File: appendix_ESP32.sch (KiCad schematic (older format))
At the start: 11 parts, among them Q301 2N3904, Q302 2N3904, SW301 SW_Push, SW302 SW_Push, U301 ESP32-WROOM-32

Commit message: fixed missing symbol issue fixed 3vout cap on FTDI
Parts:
- removed Q301, Q302: 2N3904, digikey-footprints:TO-92-3, symbol dk_Transistors-Bipolar-BJT-Single:2N3904
- added Q1, Q2: 2N3904, Package_TO_SOT_THT:TO-92_Inline, symbol Transistor_BJT:2N3904
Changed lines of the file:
@@
 	5050 4850 5050 4700
-$Comp
-L dk_Transistors-Bipolar-BJT-Single:2N3904 Q301
-U 1 1 5CBEF82D
-P 9500 2350
-F 0 "Q301" H 9688 2403 60  0000 L CNN
-F 1 "2N3904" H 9688 2297 60  0000 L CNN
-F 2 "digikey-footprints:TO-92-3" H 9700 2550 60  0001 L CNN
-F 3 "https://my.centralsemi.com/get_document.php?cmp=1&mergetype=pd&mergepath=pd&pdf_id=LSSGP072.PDF" H 9700 2650 60  0001 L CNN
-F 4 "2N3904CS-ND" H 9700 2750 60  0001 L CNN "Digi-Key_PN"
-F 5 "2N3904" H 9700 2850 60  0001 L CNN "MPN"
-F 6 "Discrete Semiconductor Products" H 9700 2950 60  0001 L CNN "Category"
-F 7 "Transistors - Bipolar (BJT) - Single" H 9700 3050 60  0001 L CNN "Family"
-F 8 "https://my.centralsemi.com/get_document.php?cmp=1&mergetype=pd&mergepath=pd&pdf_id=LSSGP072.PDF" H 9700 3150 60  0001 L CNN "DK_Datasheet_Link"
-F 9 "/product-detail/en/central-semiconductor-corp/2N3904/2N3904CS-ND/4806876" H 9700 3250 60  0001 L CNN "DK_Detail_Page"
-F 10 "TRANS NPN 40V TO-92" H 9700 3350 60  0001 L CNN "Description"
-F 11 "Central Semiconductor Corp" H 9700 3450 60  0001 L CNN "Manufacturer"
-F 12 "Active" H 9700 3550 60  0001 L CNN "Status"
-	1    9500 2350
-	1    0    0    -1
-$EndComp
-$Comp
-L dk_Transistors-Bipolar-BJT-Single:2N3904 Q302
-U 1 1 5CBF1B4A
-P 9500 3000
-F 0 "Q302" H 9688 2947 60  0000 L CNN
-F 1 "2N3904" H 9688 3053 60  0000 L CNN
-F 2 "digikey-footprints:TO-92-3" H 9700 3200 60  0001 L CNN
-F 3 "https://my.centralsemi.com/get_document.php?cmp=1&mergetype=pd&mergepath=pd&pdf_id=LSSGP072.PDF" H 9700 3300 60  0001 L CNN
-F 4 "2N3904CS-ND" H 9700 3400 60  0001 L CNN "Digi-Key_PN"
-F 5 "2N3904" H 9700 3500 60  0001 L CNN "MPN"
-F 6 "Discrete Semiconductor Products" H 9700 3600 60  0001 L CNN "Category"
-F 7 "Transistors - Bipolar (BJT) - Single" H 9700 3700 60  0001 L CNN "Family"
-F 8 "https://my.centralsemi.com/get_document.php?cmp=1&mergetype=pd&mergepath=pd&pdf_id=LSSGP072.PDF" H 9700 3800 60  0001 L CNN "DK_Datasheet_Link"
-F 9 "/product-detail/en/central-semiconductor-corp/2N3904/2N3904CS-ND/4806876" H 9700 3900 60  0001 L CNN "DK_Detail_Page"
-F 10 "TRANS NPN 40V TO-92" H 9700 4000 60  0001 L CNN "Description"
-F 11 "Central Semiconductor Corp" H 9700 4100 60  0001 L CNN "Manufacturer"
-F 12 "Active" H 9700 4200 60  0001 L CNN "Status"
-	1    9500 3000
-	1    0    0    1
-$EndComp
 $Comp
 L Device:R R302
@@
 EndData
 $EndBitmap
+$Comp
+L Transistor_BJT:2N3904 Q1
+U 1 1 5CBE1CFC
+P 9500 2350
+F 0 "Q1" H 9690 2396 50  0000 L CNN
+F 1 "2N3904" H 9690 2305 50  0000 L CNN
+F 2 "Package_TO_SOT_THT:TO-92_Inline" H 9700 2275 50  0001 L CIN
+F 3 "https://www.fairchildsemi.com/datasheets/2N/2N3904.pdf" H 9500 2350 50  0001 L CNN
+	1    9500 2350
+	1    0    0    -1
+$EndComp
+$Comp
+L Transistor_BJT:2N3904 Q2
+U 1 1 5CBE30DA
+P 9500 3000
+F 0 "Q2" H 9690 2954 50  0000 L CNN
+F 1 "2N3904" H 9690 3045 50  0000 L CNN
+F 2 "Package_TO_SOT_THT:TO-92_Inline" H 9700 2925 50  0001 L CIN
+F 3 "https://www.fairchildsemi.com/datasheets/2N/2N3904.pdf" H 9500 3000 50  0001 L CNN
+	1    9500 3000
+	1    0    0    1
+$EndComp
 $EndSCHEMATC

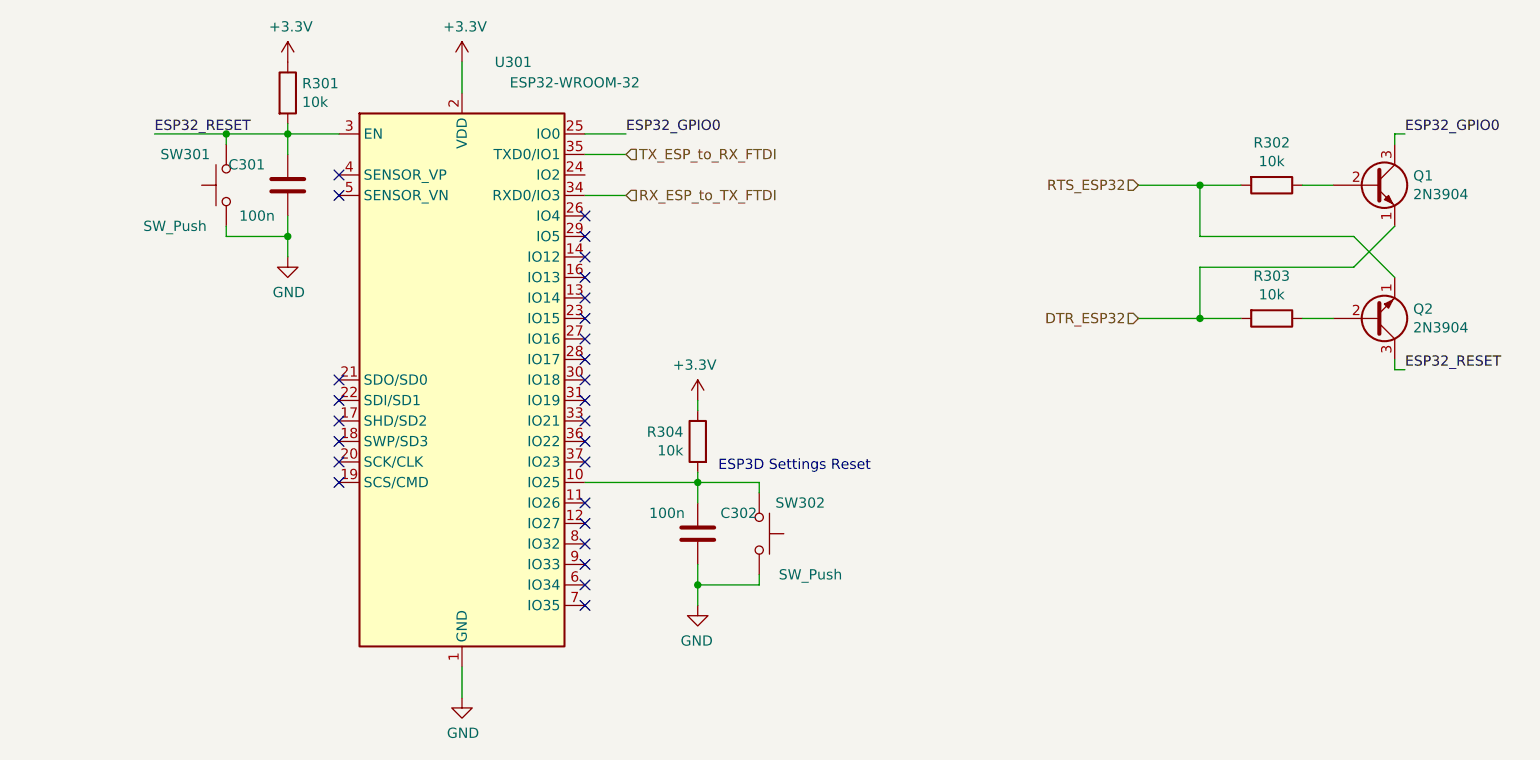
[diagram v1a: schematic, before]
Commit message: started with STM32 Pinout connections (Mittagspause)
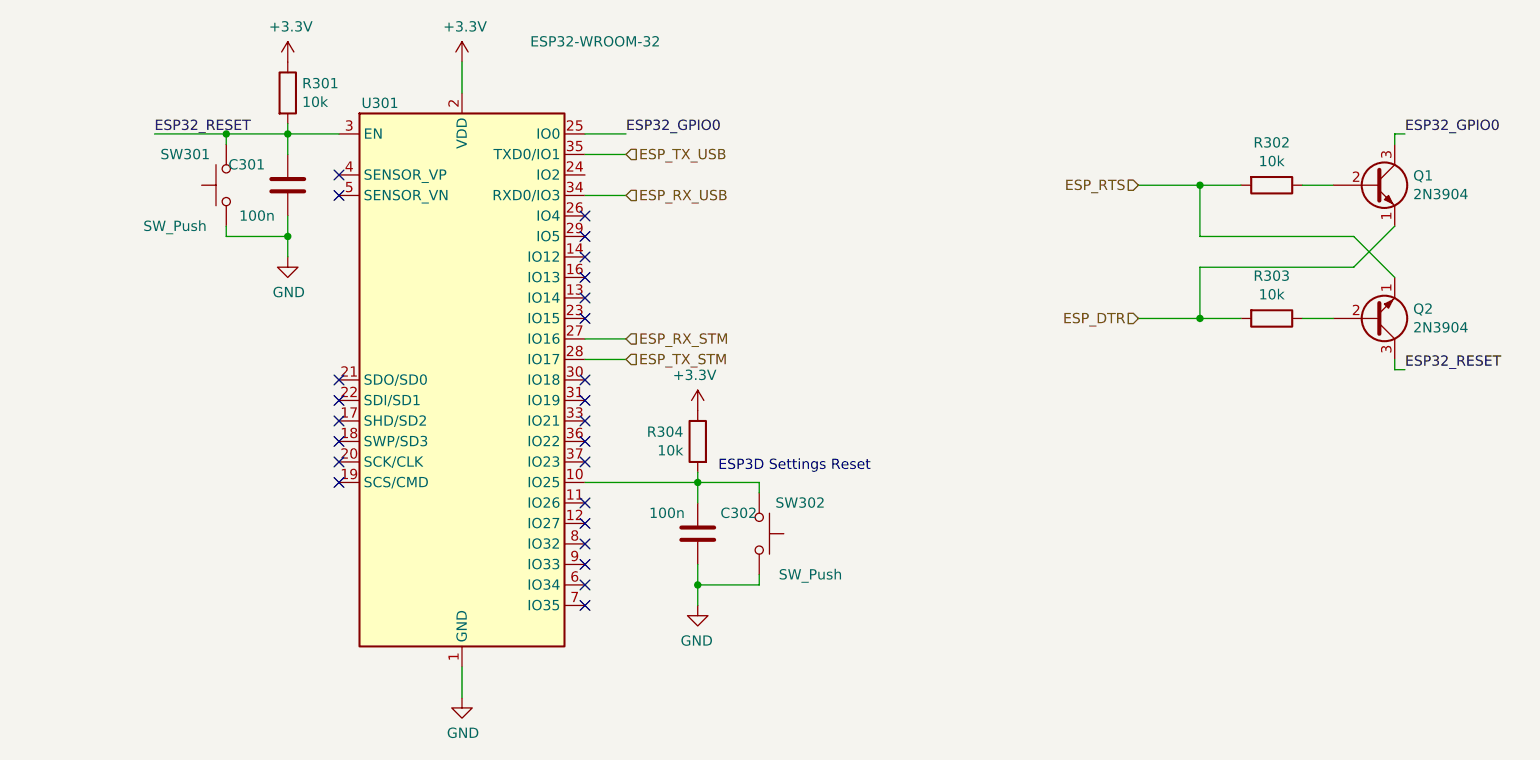
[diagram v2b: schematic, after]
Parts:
- Q1, Q2: footprint Package_TO_SOT_THT:TO-92_Inline -> TO_SOT_Packages_SMD:SOT-23
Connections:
- net ESP_RX_STM: now reaches U301.27 (IO16)
- net ESP_TX_STM: now reaches U301.28 (IO17)
- net DTR_ESP32 renamed ESP_DTR
- net RTS_ESP32 renamed ESP_RTS
- net RX_ESP_to_TX_FTDI renamed ESP_RX_USB
- net TX_ESP_to_RX_FTDI renamed ESP_TX_USB
- no-connect marks 27 -> 25

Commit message: having issues with netclasses
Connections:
- no-connect marks 25 -> 26
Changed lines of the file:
@@
 Text HLabel 5850 3200 2    50   Input ~ 0
 ESP_TX_STM
+NoConn ~ 5650 2300
 $EndSCHEMATC

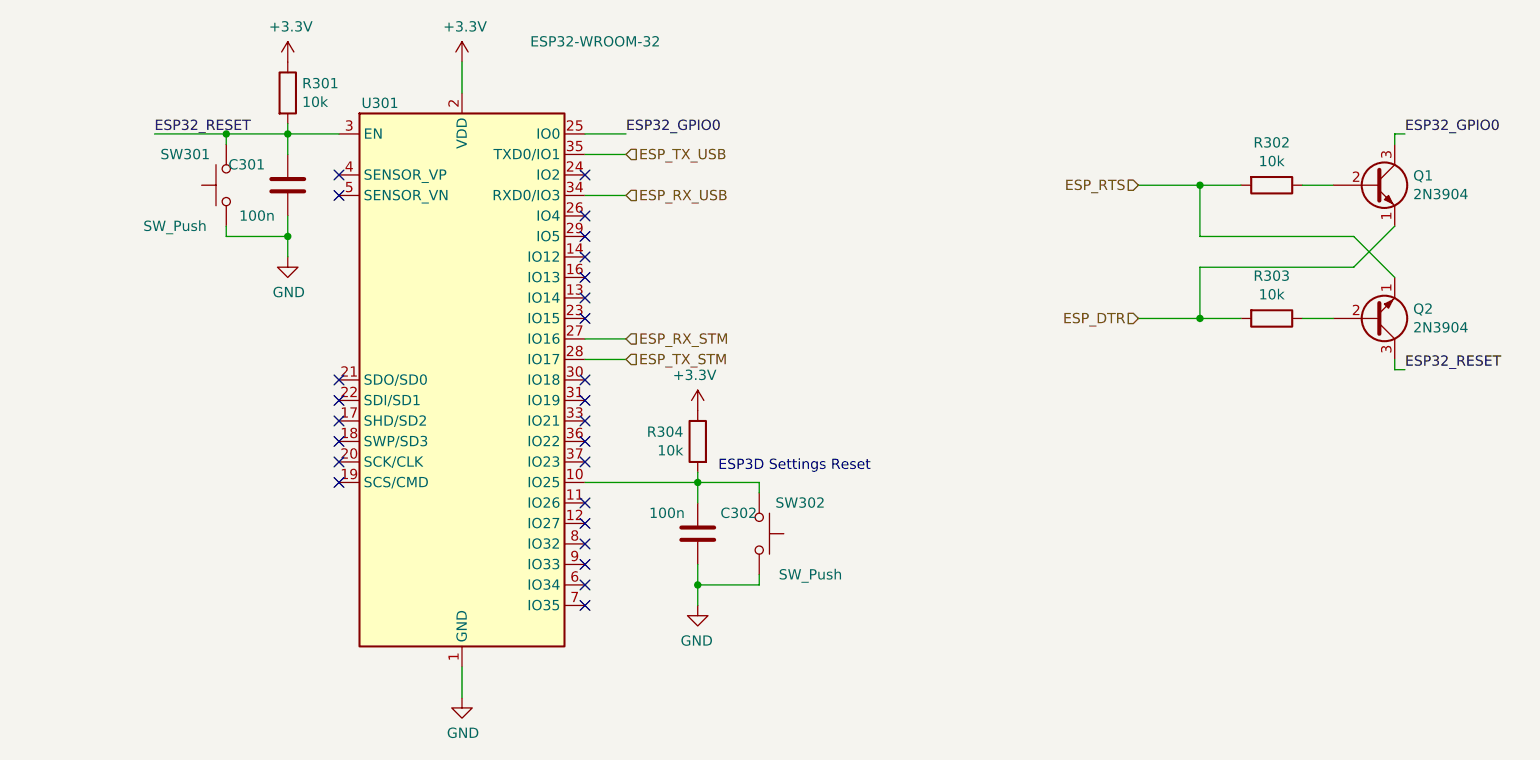
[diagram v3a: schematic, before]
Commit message: TVS protection, BOOT1 pin, user BTN
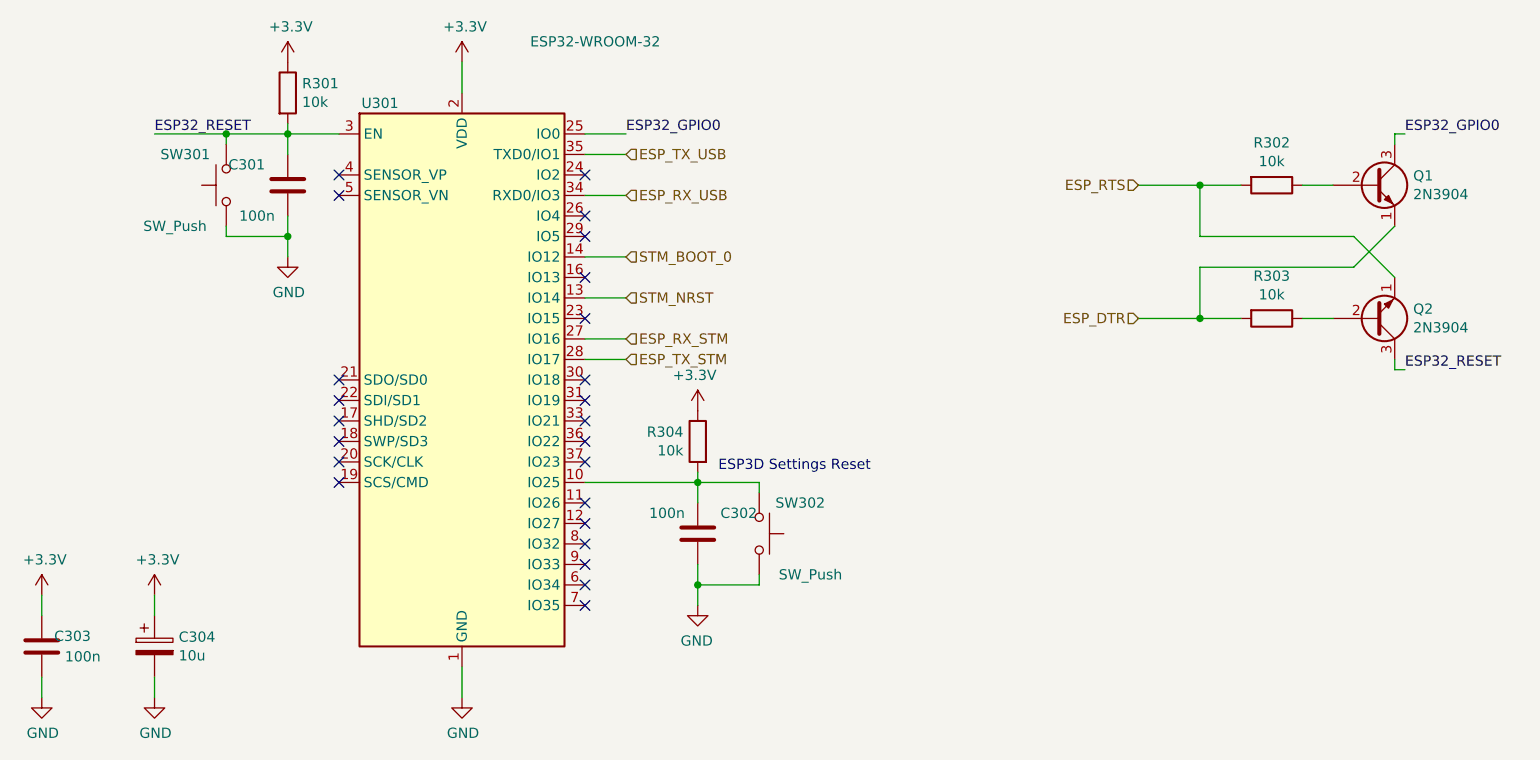
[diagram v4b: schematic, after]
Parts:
- added C303: 100n, Capacitors_SMD:C_0603, symbol Device:C
- added C304: 10u, Capacitors_SMD:C_1210, symbol Device:CP
- SW301, SW302: footprint Button_Switch_SMD:SW_SPST_KMR2 -> Buttons_Switches_SMD:SW_SPST_KMR2
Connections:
- net +3V3: now also C303.1, C304.1
- net GND: now also C303.2, C304.2
- net STM_NRST: now reaches U301.13 (IO14)
- net STM_BOOT_0: now reaches U301.14 (IO12)
- no-connect marks 26 -> 24
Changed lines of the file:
@@
 F 0 "SW302" V 6650 4250 50  0000 C CNN
 F 1 "SW_Push" V 6300 4300 50  0000 C CNN
-F 2 "Button_Switch_SMD:SW_SPST_KMR2" H 6500 4250 50  0001 C CNN
+F 2 "Buttons_Switches_SMD:SW_SPST_KMR2" H 6500 4250 50  0001 C CNN
 F 3 "~" H 6500 4250 50  0001 C CNN
 	1    6500 4050
@@
 F 0 "SW301" V 4050 2550 50  0000 C CNN
 F 1 "SW_Push" V 3700 2600 50  0000 C CNN
-F 2 "Button_Switch_SMD:SW_SPST_KMR2" H 3900 2550 50  0001 C CNN
+F 2 "Buttons_Switches_SMD:SW_SPST_KMR2" H 3900 2550 50  0001 C CNN
 F 3 "~" H 3900 2550 50  0001 C CNN
 	1    3900 2350
@@
 NoConn ~ 5650 3300
 NoConn ~ 5650 3000
-NoConn ~ 5650 2900
 NoConn ~ 5650 2800
-NoConn ~ 5650 2700
 NoConn ~ 5650 2600
 NoConn ~ 5650 2500
@@
 ESP_TX_STM
 NoConn ~ 5650 2300
+$Comp
+L power:GND #PWR?
+U 1 1 5D7E31F6
+P 3550 4850
+AR Path="/5CA3CC17/5D7E31F6" Ref="#PWR?"  Part="1"
+AR Path="/5CA3954A/5D7E31F6" Ref="#PWR?"  Part="1"
+AR Path="/5CA395A8/5D7E31F6" Ref="#PWR0307"  Part="1"
+F 0 "#PWR0307" H 3550 4600 50  0001 C CNN
+F 1 "GND" H 3555 4677 50  0000 C CNN
+F 2 "" H 3550 4850 50  0001 C CNN
+F 3 "" H 3550 4850 50  0001 C CNN
+	1    3550 4850
+	1    0    0    -1
+$EndComp
+Wire Wire Line
+	3550 4450 3550 4350
+Wire Wire Line
+	3550 4850 3550 4750
+$Comp
+L Device:CP C?
+U 1 1 5D7E31FE
+P 3550 4600
+AR Path="/5CA3CC17/5D7E31FE" Ref="C?"  Part="1"
+AR Path="/5CA3954A/5D7E31FE" Ref="C?"  Part="1"
+AR Path="/5CA395A8/5D7E31FE" Ref="C304"  Part="1"
+F 0 "C304" H 3668 4646 50  0000 L CNN
+F 1 "10u" H 3668 4555 50  0000 L CNN
+F 2 "Capacitors_SMD:C_1210" H 3588 4450 50  0001 C CNN
+F 3 "~" H 3550 4600 50  0001 C CNN
+	1    3550 4600
+	1    0    0    -1
+$EndComp
+$Comp
+L power:+3.3V #PWR?
+U 1 1 5D7E3204
+P 3550 4350
+AR Path="/5CA3954A/5D7E3204" Ref="#PWR?"  Part="1"
+AR Path="/5CA395A8/5D7E3204" Ref="#PWR0305"  Part="1"
+F 0 "#PWR0305" H 3550 4200 50  0001 C CNN
+F 1 "+3.3V" H 3565 4523 50  0000 C CNN
+F 2 "" H 3550 4350 50  0001 C CNN
+F 3 "" H 3550 4350 50  0001 C CNN
+	1    3550 4350
+	1    0    0    -1
+$EndComp
+$Comp
+L power:GND #PWR?
+U 1 1 5D7E3B0F
+P 3000 4850
+AR Path="/5CA3CC17/5D7E3B0F" Ref="#PWR?"  Part="1"
+AR Path="/5CA3954A/5D7E3B0F" Ref="#PWR?"  Part="1"
+AR Path="/5CA395A8/5D7E3B0F" Ref="#PWR0306"  Part="1"
+F 0 "#PWR0306" H 3000 4600 50  0001 C CNN
+F 1 "GND" H 3005 4677 50  0000 C CNN
+F 2 "" H 3000 4850 50  0001 C CNN
+F 3 "" H 3000 4850 50  0001 C CNN
+	1    3000 4850
+	1    0    0    -1
+$EndComp
+Wire Wire Line
+	3000 4450 3000 4350
+Wire Wire Line
+	3000 4850 3000 4750
+$Comp
+L power:+3.3V #PWR?
+U 1 1 5D7E3B25
+P 3000 4350
+AR Path="/5CA3954A/5D7E3B25" Ref="#PWR?"  Part="1"
+AR Path="/5CA395A8/5D7E3B25" Ref="#PWR0304"  Part="1"
+F 0 "#PWR0304" H 3000 4200 50  0001 C CNN
+F 1 "+3.3V" H 3015 4523 50  0000 C CNN
+F 2 "" H 3000 4350 50  0001 C CNN
+F 3 "" H 3000 4350 50  0001 C CNN
+	1    3000 4350
+	1    0    0    -1
+$EndComp
+$Comp
+L Device:C C?
+U 1 1 5D7E529A
+P 3000 4600
+AR Path="/5CA3954A/5D7E529A" Ref="C?"  Part="1"
+AR Path="/5CA395A8/5D7E529A" Ref="C303"  Part="1"
+F 0 "C303" H 2850 4650 50  0000 C CNN
+F 1 "100n" H 2800 4550 50  0000 C CNN
+F 2 "Capacitors_SMD:C_0603" H 3038 4450 50  0001 C CNN
+F 3 "~" H 3000 4600 50  0001 C CNN
+	1    3000 4600
+	-1   0    0    -1
+$EndComp
+Text HLabel 5850 2900 2    50   Input ~ 0
+STM_NRST
+Text HLabel 5850 2700 2    50   Input ~ 0
+STM_BOOT_0
+Wire Wire Line
+	5850 2900 5650 2900
+Wire Wire Line
+	5850 2700 5650 2700
 $EndSCHEMATC

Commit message: Added comments to the schematic. Changed various component values (annotated only).
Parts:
- C301, C302, C303: symbol Device:C -> FHNW-Pro4E-FS19T8-3DPrinterBoard-STM32-rescue:C-Device
- C304: symbol Device:CP -> FHNW-Pro4E-FS19T8-3DPrinterBoard-STM32-rescue:CP-Device
- Q1, Q2: symbol Transistor_BJT:2N3904 -> FHNW-Pro4E-FS19T8-3DPrinterBoard-STM32-rescue:2N3904-Transistor_BJT
- R301, R302, R303, R304: symbol Device:R -> FHNW-Pro4E-FS19T8-3DPrinterBoard-STM32-rescue:R-Device
- SW301, SW302: symbol Switch:SW_Push -> FHNW-Pro4E-FS19T8-3DPrinterBoard-STM32-rescue:SW_Push-Switch
- U301: symbol RF_Module:ESP32-WROOM-32 -> FHNW-Pro4E-FS19T8-3DPrinterBoard-STM32-rescue:ESP32-WROOM-32-RF_Module
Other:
- note added: "DTR RTS => EN IO0\n-------------\n 1 1 1 1\n 0 0 1 1\n 1 0 0 1\n 0 1 1 0"
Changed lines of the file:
@@
 $EndDescr
 $Comp
-L power:GND #PWR0136
+L FHNW-Pro4E-FS19T8-3DPrinterBoard-STM32-rescue:GND-power #PWR0136
 U 1 1 5CA3C9F2
 P 5050 4850
@@
 $EndComp
 $Comp
-L power:+3.3V #PWR0137
+L FHNW-Pro4E-FS19T8-3DPrinterBoard-STM32-rescue:+3.3V-power #PWR0137
 U 1 1 5CA3CA30
 P 5050 1750
@@
 $EndComp
 $Comp
-L RF_Module:ESP32-WROOM-32 U301
+L FHNW-Pro4E-FS19T8-3DPrinterBoard-STM32-rescue:ESP32-WROOM-32-RF_Module U301
 U 1 1 5CA47080
 P 5050 3300
@@
 	5050 4850 5050 4700
 $Comp
-L Device:R R302
+L FHNW-Pro4E-FS19T8-3DPrinterBoard-STM32-rescue:R-Device R302
 U 1 1 5CBF31BB
 P 9000 2350
@@
 $EndComp
 $Comp
-L Device:R R303
+L FHNW-Pro4E-FS19T8-3DPrinterBoard-STM32-rescue:R-Device R303
 U 1 1 5CBF3EA7
 P 9000 3000
@@
 ESP32_RESET
 $Comp
-L Device:R R301
+L FHNW-Pro4E-FS19T8-3DPrinterBoard-STM32-rescue:R-Device R301
 U 1 1 5CBFAC95
 P 4200 1900
@@
 $EndComp
 $Comp
-L power:+3.3V #PWR0138
+L FHNW-Pro4E-FS19T8-3DPrinterBoard-STM32-rescue:+3.3V-power #PWR0138
 U 1 1 5CBFC50E
 P 4200 1750
@@
 ESP3D Settings Reset
 $Comp
-L Switch:SW_Push SW?
+L FHNW-Pro4E-FS19T8-3DPrinterBoard-STM32-rescue:SW_Push-Switch SW?
 U 1 1 5CD80C30
 P 6500 4050
@@
 $EndComp
 $Comp
-L Device:C C?
+L FHNW-Pro4E-FS19T8-3DPrinterBoard-STM32-rescue:C-Device C?
 U 1 1 5CD80C36
 P 6200 4050
@@
 $EndComp
 $Comp
-L power:GND #PWR?
+L FHNW-Pro4E-FS19T8-3DPrinterBoard-STM32-rescue:GND-power #PWR?
 U 1 1 5CD80C3C
 P 6200 4400
@@
 Connection ~ 6200 3800
 $Comp
-L Device:R R?
+L FHNW-Pro4E-FS19T8-3DPrinterBoard-STM32-rescue:R-Device R?
 U 1 1 5CD80C4C
 P 6200 3600
@@
 	6200 3800 6200 3750
 $Comp
-L power:+3.3V #PWR?
+L FHNW-Pro4E-FS19T8-3DPrinterBoard-STM32-rescue:+3.3V-power #PWR?
 U 1 1 5CD80C53
 P 6200 3450
@@
 NoConn ~ 4450 2400
 $Comp
-L Switch:SW_Push SW?
+L FHNW-Pro4E-FS19T8-3DPrinterBoard-STM32-rescue:SW_Push-Switch SW?
 U 1 1 5CD83394
 P 3900 2350
@@
 $EndComp
 $Comp
-L Device:C C?
+L FHNW-Pro4E-FS19T8-3DPrinterBoard-STM32-rescue:C-Device C?
 U 1 1 5CD8339E
 P 4200 2350
@@
 $EndComp
 $Comp
-L power:GND #PWR?
+L FHNW-Pro4E-FS19T8-3DPrinterBoard-STM32-rescue:GND-power #PWR?
 U 1 1 5CD833A8
 P 4200 2700
@@
 $EndBitmap
 $Comp
-L Transistor_BJT:2N3904 Q1
+L FHNW-Pro4E-FS19T8-3DPrinterBoard-STM32-rescue:2N3904-Transistor_BJT Q1
 U 1 1 5CBE1CFC
 P 9500 2350
@@
 $EndComp
 $Comp
-L Transistor_BJT:2N3904 Q2
+L FHNW-Pro4E-FS19T8-3DPrinterBoard-STM32-rescue:2N3904-Transistor_BJT Q2
 U 1 1 5CBE30DA
 P 9500 3000
@@
 NoConn ~ 5650 2300
 $Comp
-L power:GND #PWR?
+L FHNW-Pro4E-FS19T8-3DPrinterBoard-STM32-rescue:GND-power #PWR?
 U 1 1 5D7E31F6
 P 3550 4850
@@
 	3550 4850 3550 4750
 $Comp
-L Device:CP C?
+L FHNW-Pro4E-FS19T8-3DPrinterBoard-STM32-rescue:CP-Device C?
 U 1 1 5D7E31FE
 P 3550 4600
@@
 $EndComp
 $Comp
-L power:+3.3V #PWR?
+L FHNW-Pro4E-FS19T8-3DPrinterBoard-STM32-rescue:+3.3V-power #PWR?
 U 1 1 5D7E3204
 P 3550 4350
@@
 $EndComp
 $Comp
-L power:GND #PWR?
+L FHNW-Pro4E-FS19T8-3DPrinterBoard-STM32-rescue:GND-power #PWR?
 U 1 1 5D7E3B0F
 P 3000 4850
@@
 	3000 4850 3000 4750
 $Comp
-L power:+3.3V #PWR?
+L FHNW-Pro4E-FS19T8-3DPrinterBoard-STM32-rescue:+3.3V-power #PWR?
 U 1 1 5D7E3B25
 P 3000 4350
@@
 $EndComp
 $Comp
-L Device:C C?
+L FHNW-Pro4E-FS19T8-3DPrinterBoard-STM32-rescue:C-Device C?
 U 1 1 5D7E529A
 P 3000 4600
@@
 Wire Wire Line
 	5850 2700 5650 2700
+Text Notes 8700 4050 0    50   ~ 10
+DTR RTS => EN IO0\n-------------\n 1   1        1  1\n 0   0        1  1\n 1   0        0  1\n 0   1        1  0
 $EndSCHEMATC
